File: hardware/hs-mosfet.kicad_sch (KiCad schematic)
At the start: 33 parts, among them Q301 IRLML6402, Q302 2N7002

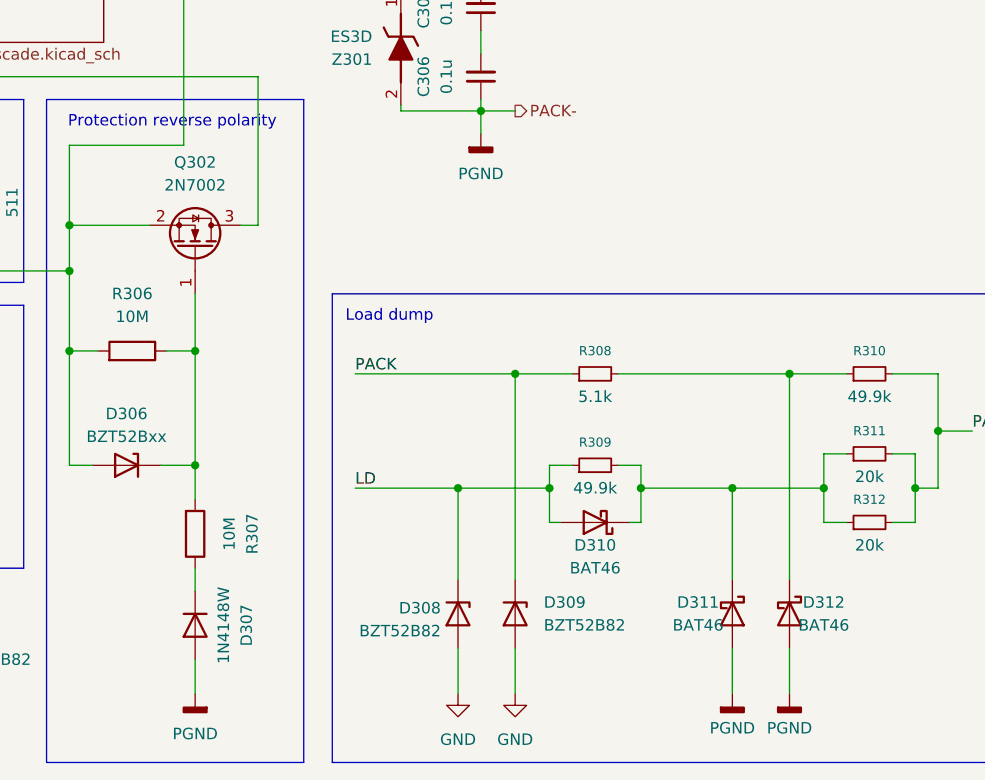
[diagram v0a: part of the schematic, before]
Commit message: fix ERC warnings and footprint issues
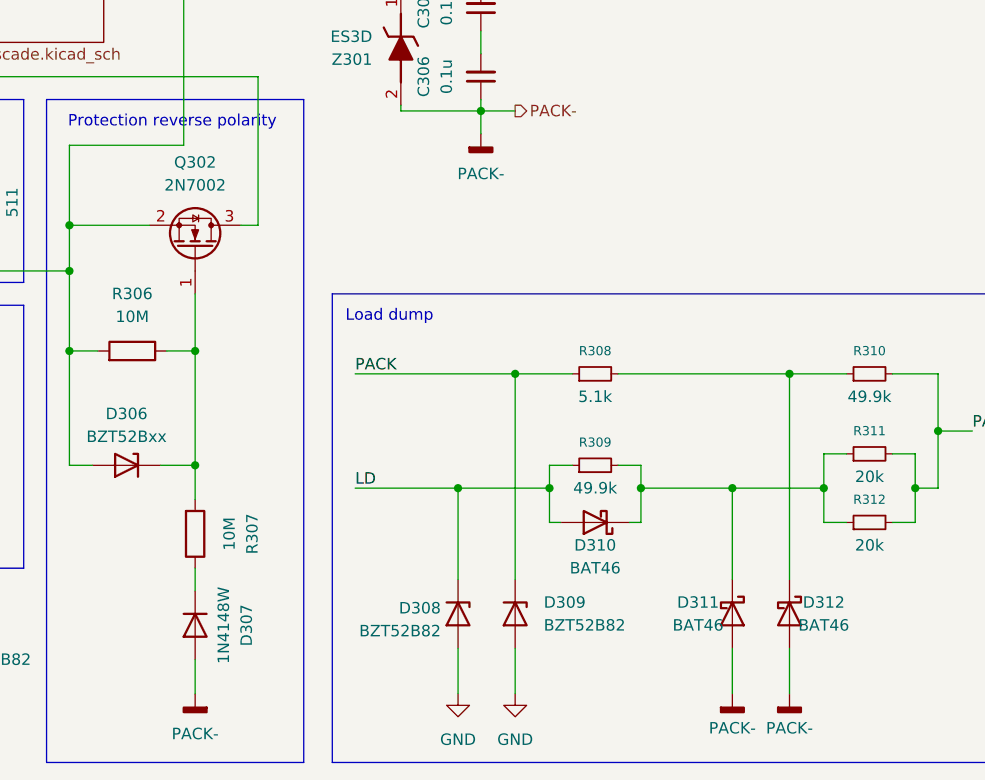
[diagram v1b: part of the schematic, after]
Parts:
- D301: footprint Samacsys:DIOM5436X265N -> Diode_SMD:D_SMB
- Z301: footprint Samacsys:DIOM8059X265N -> Diode_SMD:D_SMC
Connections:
- net PGND renamed PACK-

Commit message: update schematics
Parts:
- D301: footprint Diode_SMD:D_SMB -> Samacsys:DIOM5436X265N
- Z301: footprint Diode_SMD:D_SMC -> Samacsys:DIOM8059X265N
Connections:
- net PACK- renamed PGND

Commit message: fix remaining missing footprints
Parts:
- D301: footprint Samacsys:DIOM5436X265N -> Diode_SMD:D_SMB
- Z301: footprint Samacsys:DIOM8059X265N -> Diode_SMD:D_SMC
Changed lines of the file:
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@@
 			)
 		)
-		(property "Footprint" "Samacsys:DIOM8059X265N"
+		(property "Footprint" "Diode_SMD:D_SMC"
 			(at 90.5 88.265 0)
 			(hide yes)
@@
 			)
 		)
-		(property "Footprint" "Samacsys:DIOM5436X265N"
+		(property "Footprint" "Diode_SMD:D_SMB"
 			(at 157.15 92.71 0)
 			(hide yes)

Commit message: placed c mosfet
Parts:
- C301, C302, C303, C304, C305, C306: footprint Capacitor_SMD:C_0805_2012Metric -> Capacitor_SMD:C_0603_1608Metric
- R301, R302, R303, R304, R305, R306, R307, R308, R309, R310, R311, R312: footprint Resistor_SMD:R_0805_2012Metric -> Resistor_SMD:R_0603_1608Metric
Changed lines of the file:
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@@
 			)
 		)
-		(property "Footprint" "Resistor_SMD:R_0805_2012Metric"
+		(property "Footprint" "Resistor_SMD:R_0603_1608Metric"
 			(at 129.032 135.255 90)
 			(hide yes)
@@
 			)
 		)
-		(property "Footprint" "Resistor_SMD:R_0805_2012Metric"
+		(property "Footprint" "Resistor_SMD:R_0603_1608Metric"
 			(at 236.22 129.54 0)
 			(hide yes)
@@
 			)
 		)
-		(property "Footprint" "Resistor_SMD:R_0805_2012Metric"
+		(property "Footprint" "Resistor_SMD:R_0603_1608Metric"
 			(at 159.512 138.43 90)
 			(hide yes)
@@
 			)
 		)
-		(property "Footprint" "Resistor_SMD:R_0805_2012Metric"
+		(property "Footprint" "Resistor_SMD:R_0603_1608Metric"
 			(at 129.032 123.19 90)
 			(hide yes)
@@
 			)
 		)
-		(property "Footprint" "Capacitor_SMD:C_0805_2012Metric"
+		(property "Footprint" "Capacitor_SMD:C_0603_1608Metric"
 			(at 74.93 82.55 0)
 			(hide yes)
@@
 			)
 		)
-		(property "Footprint" "Resistor_SMD:R_0805_2012Metric"
+		(property "Footprint" "Resistor_SMD:R_0603_1608Metric"
 			(at 123.698 123.19 90)
 			(hide yes)
@@
 			)
 		)
-		(property "Footprint" "Resistor_SMD:R_0805_2012Metric"
+		(property "Footprint" "Resistor_SMD:R_0603_1608Metric"
 			(at 205.74 130.81 0)
 			(hide yes)
@@
 			)
 		)
-		(property "Footprint" "Resistor_SMD:R_0805_2012Metric"
+		(property "Footprint" "Resistor_SMD:R_0603_1608Metric"
 			(at 154.305 119.888 90)
 			(hide yes)
@@
 			)
 		)
-		(property "Footprint" "Resistor_SMD:R_0805_2012Metric"
+		(property "Footprint" "Resistor_SMD:R_0603_1608Metric"
 			(at 135.89 101.6 0)
 			(hide yes)
@@
 			)
 		)
-		(property "Footprint" "Capacitor_SMD:C_0805_2012Metric"
+		(property "Footprint" "Capacitor_SMD:C_0603_1608Metric"
 			(at 74.93 90.17 0)
 			(hide yes)
@@
 			)
 		)
-		(property "Footprint" "Resistor_SMD:R_0805_2012Metric"
+		(property "Footprint" "Resistor_SMD:R_0603_1608Metric"
 			(at 236.22 137.16 0)
 			(hide yes)
@@
 			)
 		)
-		(property "Footprint" "Capacitor_SMD:C_0805_2012Metric"
+		(property "Footprint" "Capacitor_SMD:C_0603_1608Metric"
 			(at 193.04 87.63 0)
 			(hide yes)
@@
 			)
 		)
-		(property "Footprint" "Resistor_SMD:R_0805_2012Metric"
+		(property "Footprint" "Resistor_SMD:R_0603_1608Metric"
 			(at 92.202 93.98 90)
 			(hide yes)
@@
 			)
 		)
-		(property "Footprint" "Capacitor_SMD:C_0805_2012Metric"
+		(property "Footprint" "Capacitor_SMD:C_0603_1608Metric"
 			(at 120.015 36.83 0)
 			(hide yes)
@@
 			)
 		)
-		(property "Footprint" "Capacitor_SMD:C_0805_2012Metric"
+		(property "Footprint" "Capacitor_SMD:C_0603_1608Metric"
 			(at 193.04 80.01 0)
 			(hide yes)
@@
 			)
 		)
-		(property "Footprint" "Resistor_SMD:R_0805_2012Metric"
+		(property "Footprint" "Resistor_SMD:R_0603_1608Metric"
 			(at 205.74 120.65 0)
 			(hide yes)
@@
 			)
 		)
-		(property "Footprint" "Capacitor_SMD:C_0805_2012Metric"
+		(property "Footprint" "Capacitor_SMD:C_0603_1608Metric"
 			(at 112.395 36.83 0)
 			(hide yes)
@@
 			)
 		)
-		(property "Footprint" "Resistor_SMD:R_0805_2012Metric"
+		(property "Footprint" "Resistor_SMD:R_0603_1608Metric"
 			(at 236.22 120.65 0)
 			(hide yes)

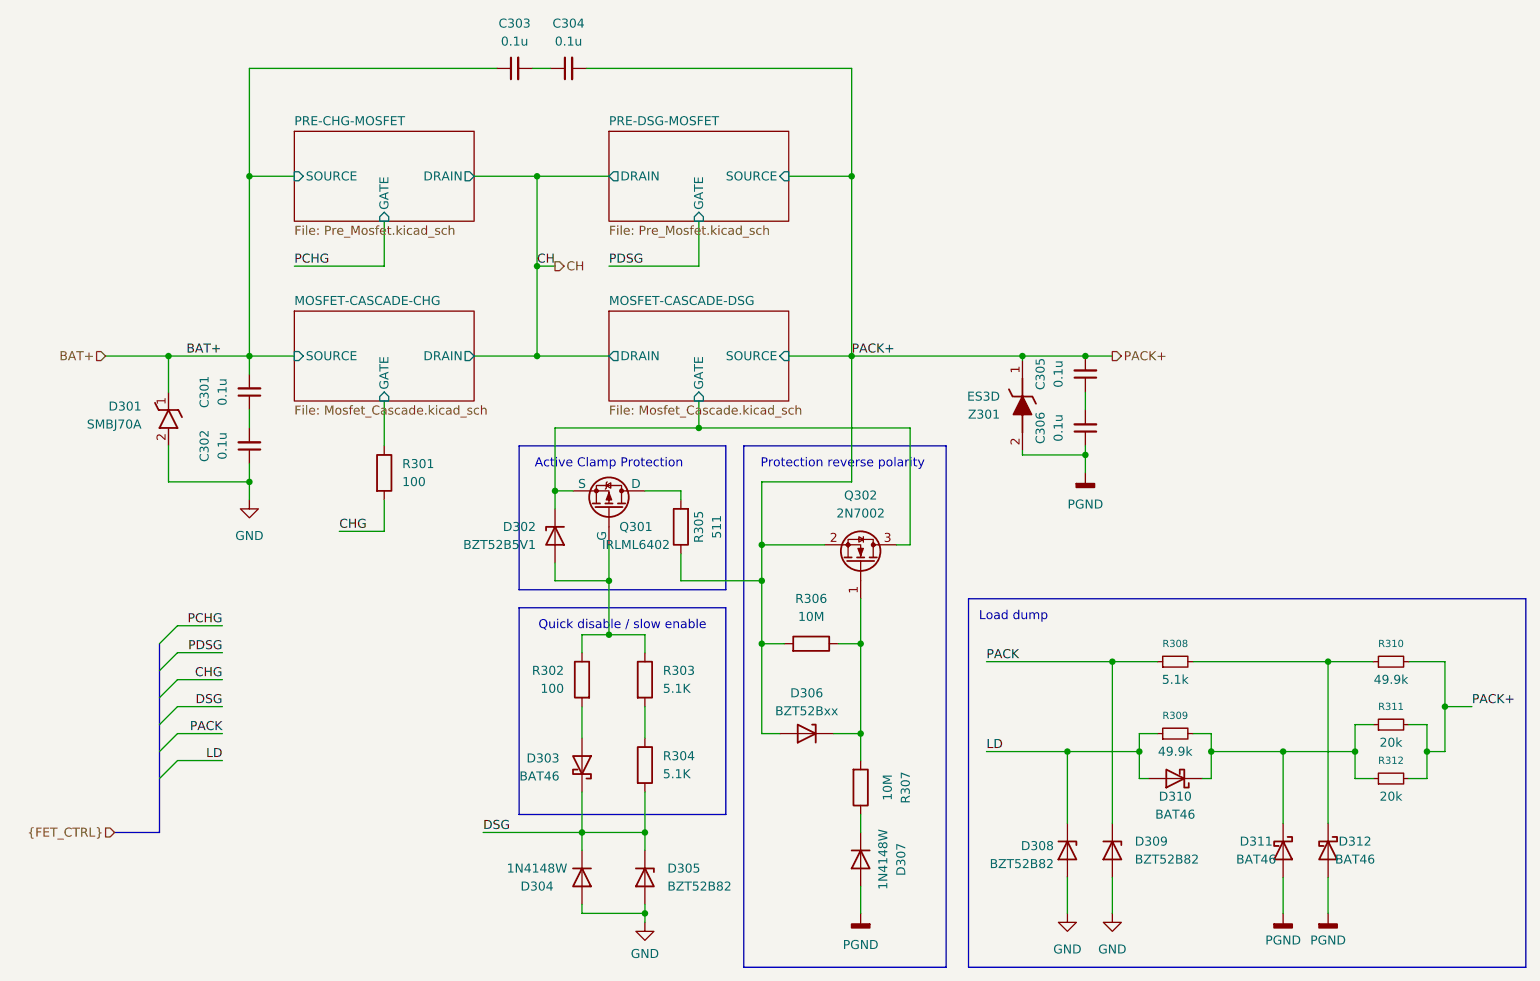
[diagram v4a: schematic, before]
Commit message: reduced BOM
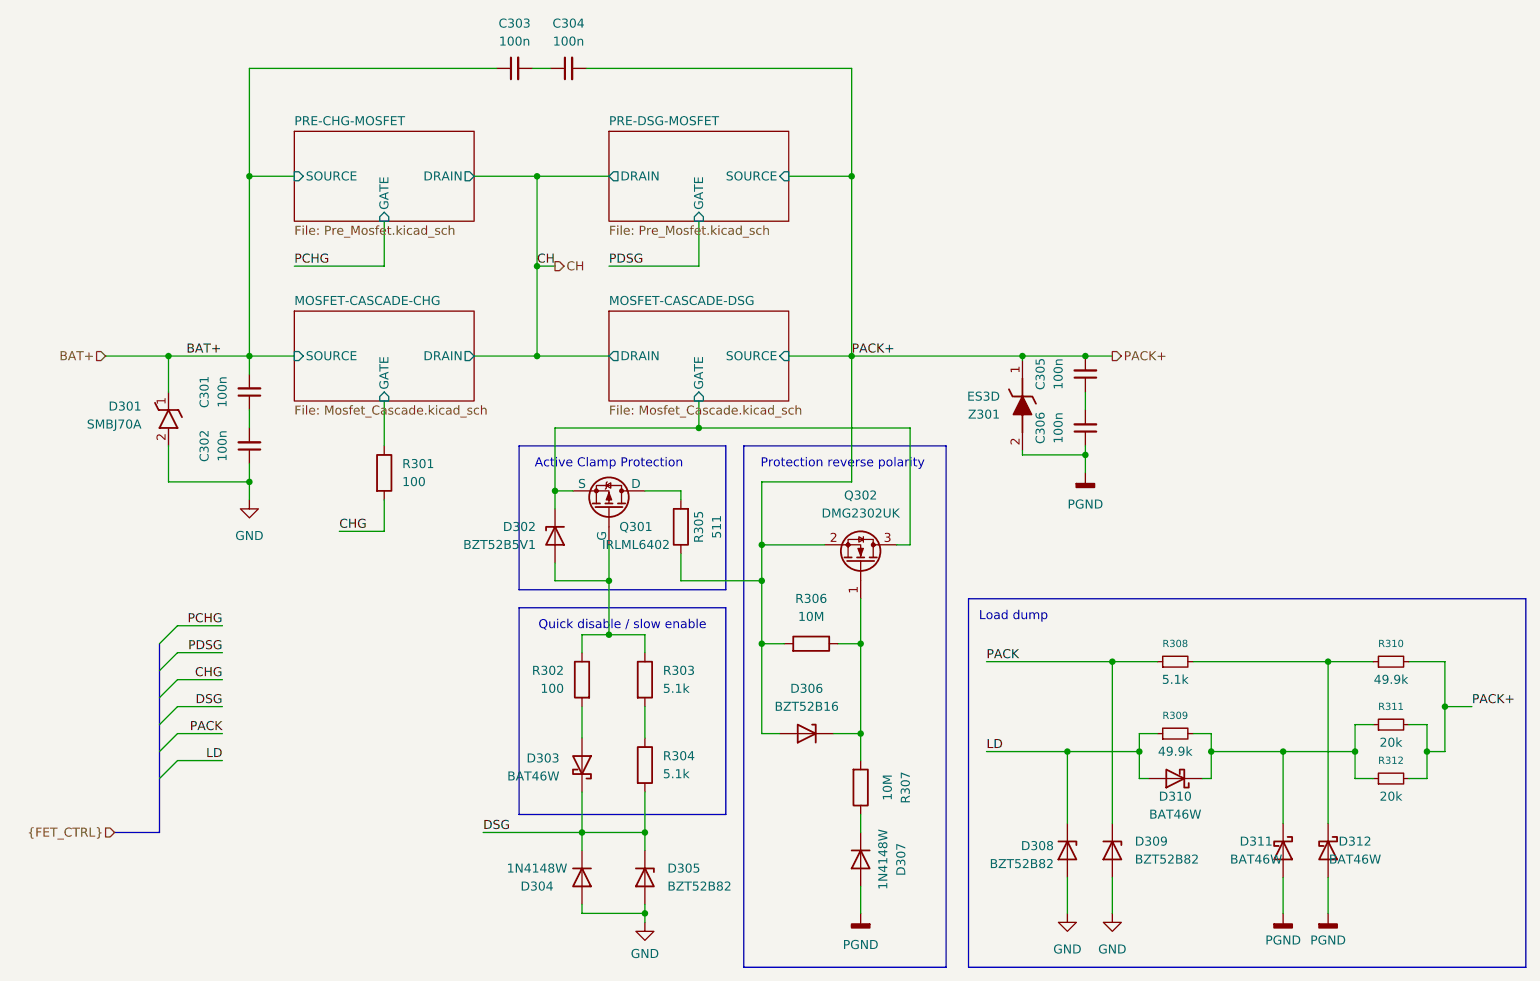
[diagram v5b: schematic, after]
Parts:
- C301, C302, C303, C304, C305, C306: value 0.1u -> 100n
- D302: footprint (none) -> Diode_SMD:D_SOD-123
- D303, D310, D311, D312: value BAT46 -> BAT46W; footprint Diode_THT:D_DO-35_SOD27_P7.62mm_Horizontal -> Diode_SMD:D_SOD-123
- D306: value BZT52Bxx -> BZT52B16
- Q302: value 2N7002 -> DMG2302UK
- R303, R304: value 5.1K -> 5.1k

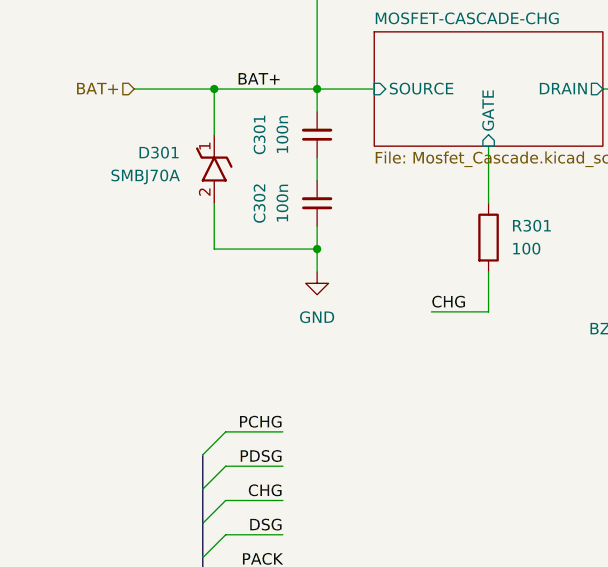
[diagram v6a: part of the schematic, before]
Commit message: Actualize resistors size
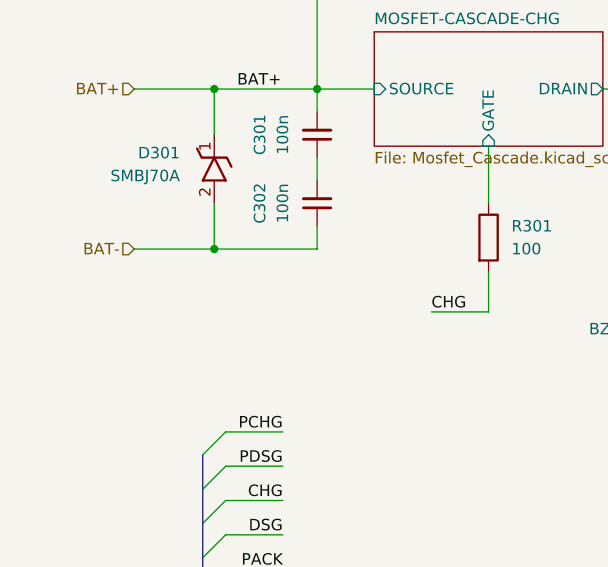
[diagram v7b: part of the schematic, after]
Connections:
- net GND: no longer C302.1, D301.2 (A)
- new net BAT-: C302.1, D301.2 (A)
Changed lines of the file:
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@@
-	)
-	(junction
-		(at 74.93 95.25)
-		(diameter 0)
-		(color 0 0 0 0)
 	)
 	(junction
@@
 	)
 	(junction
+		(at 63.5 95.25)
+		(diameter 0)
+		(color 0 0 0 0)
+	)
+	(junction
 		(at 115.57 64.77)
 		(diameter 0)
@@
 	(wire
 		(pts
-			(xy 74.93 95.25) (xy 74.93 97.79)
-		)
-		(stroke
-			(width 0)
-			(type default)
-		)
-	)
-	(wire
-		(pts
 			(xy 118.11 109.22) (xy 125.73 109.22)
 		)
@@
 		(pts
 			(xy 74.93 52.07) (xy 74.93 77.47)
+		)
+		(stroke
+			(width 0)
+			(type default)
+		)
+	)
+	(wire
+		(pts
+			(xy 54.61 95.25) (xy 63.5 95.25)
 		)
 		(stroke
@@
 		(shape input)
 		(at 54.61 77.47 180)
+		(effects
+			(font
+				(size 1.27 1.27)
+			)
+			(justify right)
+		)
+	)
+	(hierarchical_label "BAT-"
+		(shape input)
+		(at 54.61 95.25 180)
 		(effects
 			(font
@@
 					(unit 1)
 				)
-			)
-		)
-	)
-	(symbol
-		(lib_id "power:GND")
-		(at 74.93 97.79 0)
-		(unit 1)
-		(body_style 1)
-		(exclude_from_sim no)
-		(in_bom yes)
-		(on_board yes)
-		(in_pos_files yes)
-		(dnp no)
-		(fields_autoplaced yes)
-		(property "Reference" "#PWR0301"
-			(at 74.93 104.14 0)
-			(hide yes)
-			(show_name no)
-			(do_not_autoplace no)
-			(effects
-				(font
-					(size 1.27 1.27)
-				)
-			)
-		)
-		(property "Value" "GND"
-			(at 74.93 102.87 0)
-			(show_name no)
-			(do_not_autoplace no)
-			(effects
-				(font
-					(size 1.27 1.27)
-				)
-			)
-		)
-		(property "Footprint" ""
-			(at 74.93 97.79 0)
-			(hide yes)
-			(show_name no)
-			(do_not_autoplace no)
-			(effects
-				(font
-					(size 1.27 1.27)
-				)
-			)
-		)
-		(property "Datasheet" ""
-			(at 74.93 97.79 0)
-			(hide yes)
-			(show_name no)
-			(do_not_autoplace no)
-			(effects
-				(font
-					(size 1.27 1.27)
-				)
-			)
-		)
-		(property "Description" "Power symbol creates a global label with name \"GND\" , ground"
-			(at 74.93 97.79 0)
-			(hide yes)
-			(show_name no)
-			(do_not_autoplace no)
-			(effects
-				(font
-					(size 1.27 1.27)
-				)
-			)
-		)
-		(pin "1"
-		)
-		(instances
-			(project "wafel-eval-board"
-				(path "/3e668e3e-3e16-4665-a807-4735962c41d3/5ab6bc33-292e-4a51-947f-86660ef7cdb4"
-					(reference "#PWR0301")
-					(unit 1)
-				)

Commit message: some chnages
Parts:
- Q302: value DMG2302UK -> 2N7002K
